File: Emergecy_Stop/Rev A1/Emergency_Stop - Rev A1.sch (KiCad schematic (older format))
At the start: 9 parts, among them J1 XLR3, J2 XLR3, J3 CONN_01X02_FEMALE

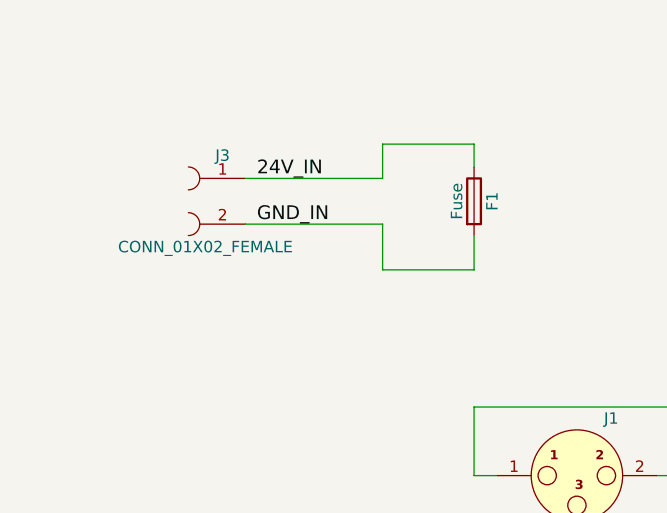
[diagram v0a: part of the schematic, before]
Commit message: Modify power connector
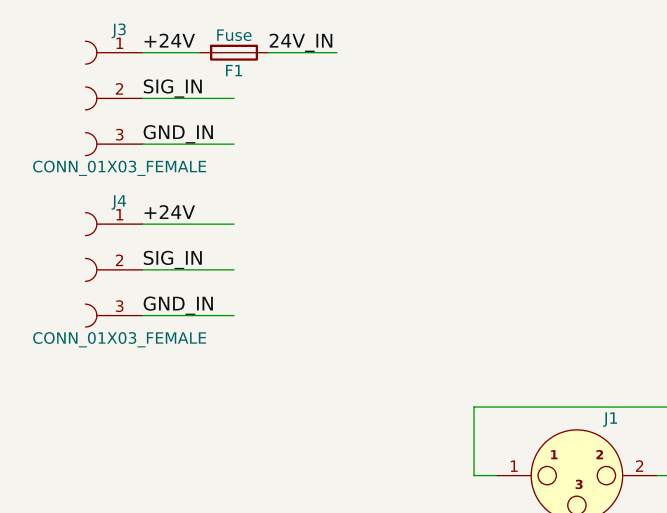
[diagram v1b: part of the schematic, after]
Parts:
- removed J3: CONN_01X02_FEMALE, test:MSTBA2.5, symbol CONN_01X02_FEMALE
- added J3: CONN_01X03_FEMALE, conn_Phoenix:MSTBA3, symbol CONN_01X03_FEMALE
- added J4: CONN_01X03_FEMALE, conn_Molex:7395-03, symbol CONN_01X03_FEMALE
- F1: footprint (none) -> Fuse:LittleFuse_1812L
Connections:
- net labels added: +24V
- wire segments 31 -> 30
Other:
- moved on the sheet: F1
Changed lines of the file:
@@
 Text Label 4500 3650 0    60   ~ 0
 GND_MECA
-Text Label 1600 1450 0    60   ~ 0
+Text Label 1650 900  0    60   ~ 0
 24V_IN
-Text Label 1600 1650 0    60   ~ 0
+Text Label 1100 1300 0    60   ~ 0
 GND_IN
 $Comp
@@
 Wire Wire Line
 	2550 2750 2550 2450
-Wire Wire Line
-	1550 1450 2150 1450
-Wire Wire Line
-	1550 1650 2150 1650
 $Comp
-L CONN_01X02_FEMALE J3
-U 1 1 591BFBFE
-P 1450 1550
-F 0 "J3" H 1450 1750 50  0000 C CNN
-F 1 "CONN_01X02_FEMALE" H 1525 1350 50  0000 C CNN
-F 2 "test:MSTBA2.5" H 1450 1650 50  0001 C CNN
-F 3 "" H 1450 1650 50  0001 C CNN
-	1    1450 1550
+L Fuse F1
+U 1 1 591C165B
+P 1500 900
+F 0 "F1" V 1580 900 50  0000 C CNN
+F 1 "Fuse" V 1425 900 50  0000 C CNN
+F 2 "Fuse:LittleFuse_1812L" V 1430 900 50  0001 C CNN
+F 3 "" H 1500 900 50  0001 C CNN
+	1    1500 900
+	0    1    1    0
+$EndComp
+Text Label 1100 1100 0    60   ~ 0
+SIG_IN
+$Comp
+L CONN_01X03_FEMALE J3
+U 1 1 591C627D
+P 1000 1100
+F 0 "J3" H 1000 1400 50  0000 C CNN
+F 1 "CONN_01X03_FEMALE" H 1000 800 50  0000 C CNN
+F 2 "conn_Phoenix:MSTBA3" H 1000 1300 50  0001 C CNN
+F 3 "" H 1000 1300 50  0001 C CNN
+	1    1000 1100
 	-1   0    0    -1
 $EndComp
 Wire Wire Line
-	2150 1450 2150 1300
+	1100 900  1350 900
 Wire Wire Line
-	2150 1300 2550 1300
+	1100 1100 1500 1100
 Wire Wire Line
-	2550 1300 2550 1400
+	1100 1300 1500 1300
 Wire Wire Line
-	2550 1700 2550 1850
+	1650 900  1950 900
+Text Label 1100 2050 0    60   ~ 0
+GND_IN
+Text Label 1100 1850 0    60   ~ 0
+SIG_IN
+$Comp
+L CONN_01X03_FEMALE J4
+U 1 1 591C6B84
+P 1000 1850
+F 0 "J4" H 1000 2150 50  0000 C CNN
+F 1 "CONN_01X03_FEMALE" H 1000 1550 50  0000 C CNN
+F 2 "conn_Molex:7395-03" H 1000 2050 50  0001 C CNN
+F 3 "" H 1000 2050 50  0001 C CNN
+	1    1000 1850
+	-1   0    0    -1
+$EndComp
 Wire Wire Line
-	2550 1850 2150 1850
+	1100 1650 1500 1650
 Wire Wire Line
-	2150 1850 2150 1650
-$Comp
-L Fuse F1
-U 1 1 591C165B
-P 2550 1550
-F 0 "F1" V 2630 1550 50  0000 C CNN
-F 1 "Fuse" V 2475 1550 50  0000 C CNN
-F 2 "" V 2480 1550 50  0001 C CNN
-F 3 "" H 2550 1550 50  0001 C CNN
-	1    2550 1550
-	1    0    0    -1
-$EndComp
+	1100 1850 1500 1850
+Wire Wire Line
+	1100 2050 1500 2050
+Text Label 1100 1650 0    60   ~ 0
++24V
+Text Label 1100 900  0    60   ~ 0
++24V
 $EndSCHEMATC

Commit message: Finishing emergency stop board and generate MDP folder
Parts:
- F1: value Fuse -> 1812L110/24DR
- J3: value CONN_01X03_FEMALE -> MSTBA2.5/3
- J4: value CONN_01X03_FEMALE -> 22-05-7038; footprint conn_Molex:7395-03 -> conn_Molex:22-05-7038
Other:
- moved on the sheet: F1
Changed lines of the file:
@@
 Text Label 4500 3650 0    60   ~ 0
 GND_MECA
-Text Label 1650 900  0    60   ~ 0
+Text Label 2050 900  0    60   ~ 0
 24V_IN
 Text Label 1100 1300 0    60   ~ 0
@@
 L Fuse F1
 U 1 1 591C165B
-P 1500 900
-F 0 "F1" V 1580 900 50  0000 C CNN
-F 1 "Fuse" V 1425 900 50  0000 C CNN
-F 2 "Fuse:LittleFuse_1812L" V 1430 900 50  0001 C CNN
-F 3 "" H 1500 900 50  0001 C CNN
-	1    1500 900
+P 1700 900
+F 0 "F1" V 1780 900 50  0000 C CNN
+F 1 "1812L110/24DR" V 1625 900 50  0000 C CNN
+F 2 "Fuse:LittleFuse_1812L" V 1630 900 50  0001 C CNN
+F 3 "" H 1700 900 50  0001 C CNN
+	1    1700 900
 	0    1    1    0
 $EndComp
@@
 P 1000 1100
 F 0 "J3" H 1000 1400 50  0000 C CNN
-F 1 "CONN_01X03_FEMALE" H 1000 800 50  0000 C CNN
+F 1 "MSTBA2.5/3" H 1000 800 50  0000 C CNN
 F 2 "conn_Phoenix:MSTBA3" H 1000 1300 50  0001 C CNN
 F 3 "" H 1000 1300 50  0001 C CNN
@@
 $EndComp
 Wire Wire Line
-	1100 900  1350 900
+	1100 900  1550 900
 Wire Wire Line
 	1100 1100 1500 1100
@@
 	1100 1300 1500 1300
 Wire Wire Line
-	1650 900  1950 900
+	1850 900  2500 900
 Text Label 1100 2050 0    60   ~ 0
 GND_IN
@@
 P 1000 1850
 F 0 "J4" H 1000 2150 50  0000 C CNN
-F 1 "CONN_01X03_FEMALE" H 1000 1550 50  0000 C CNN
-F 2 "conn_Molex:7395-03" H 1000 2050 50  0001 C CNN
+F 1 "22-05-7038" H 1000 1550 50  0000 C CNN
+F 2 "conn_Molex:22-05-7038" H 1000 2050 50  0001 C CNN
 F 3 "" H 1000 2050 50  0001 C CNN
 	1    1000 1850

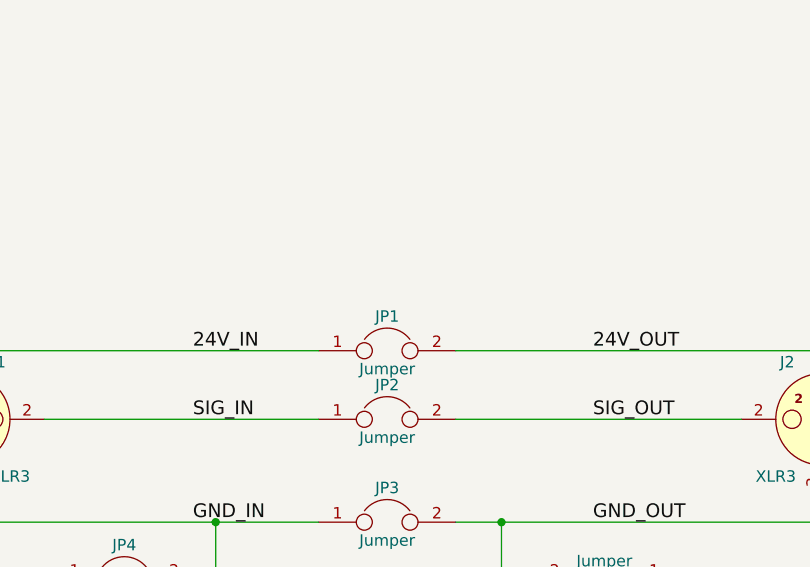
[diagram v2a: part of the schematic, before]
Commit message: Create Rev A2 of Emergency Stop board
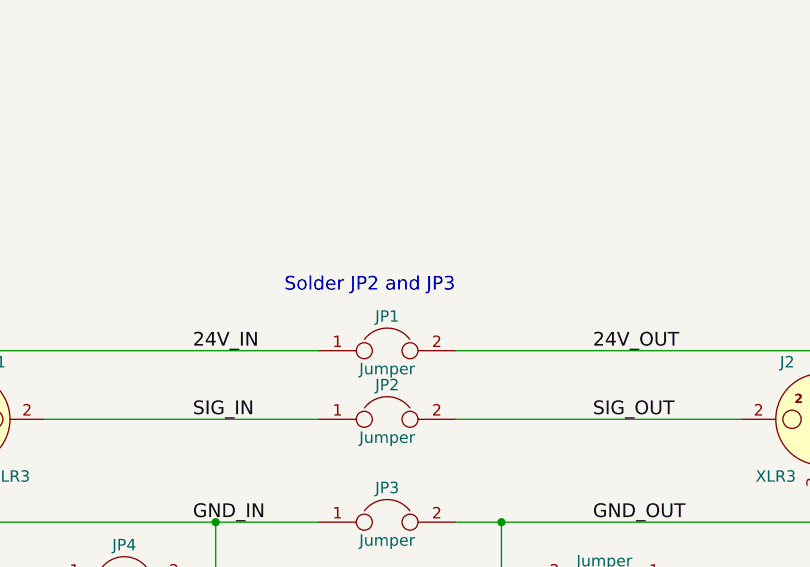
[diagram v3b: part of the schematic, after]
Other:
- note added: "Solder JP2 and JP3"
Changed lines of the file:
@@
 Text Label 1100 900  0    60   ~ 0
 +24V
+Text Notes 4400 2200 0    60   ~ 0
+Solder JP2 and JP3
 $EndSCHEMATC
